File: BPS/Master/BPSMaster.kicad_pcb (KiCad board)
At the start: 2 copper layers, 100 x 75 mm, 151 parts, among them J1 SWD, J10 CurrentSlaveConnector, J11 USB_B_Micro, J12 Conn_01x06, J13 CAN Analyzer, J14 Conn_01x06, J15 Conn_01x06, J16 Conn_01x06, J2 CarPowerConnector, J3 FrontFans, J4 BackFans, J5 SPI Analyzer, J6 VoltageSlaveConnector, J7 ContactorConnector, J8 CAN_Out, J9 ErrorLightConnector, Q1 VND5N07-E, Q2 NTR4003NT1G, Q3 NTR4003NT1G, Q4 NTR4003NT1G, Q6 DMP3013SFV, SW1 B3SL-1002P, SW3 SW_Push, U1 STM32F413RHTx, U10 BAS70-04, U11 SI8261ABC-IS, U12 CDSOT23-T24CAN, U13 ADM3055E, U14 SI8261ABC-IS, U15 CP2102N-A01-GQFN24, U2 RI3-1205S, U3 NCP1117-3.3_SOT223, U4 M24128, U5 LTC6256, U8 LTC6820, U9 HX1188FNL, Y1 8M

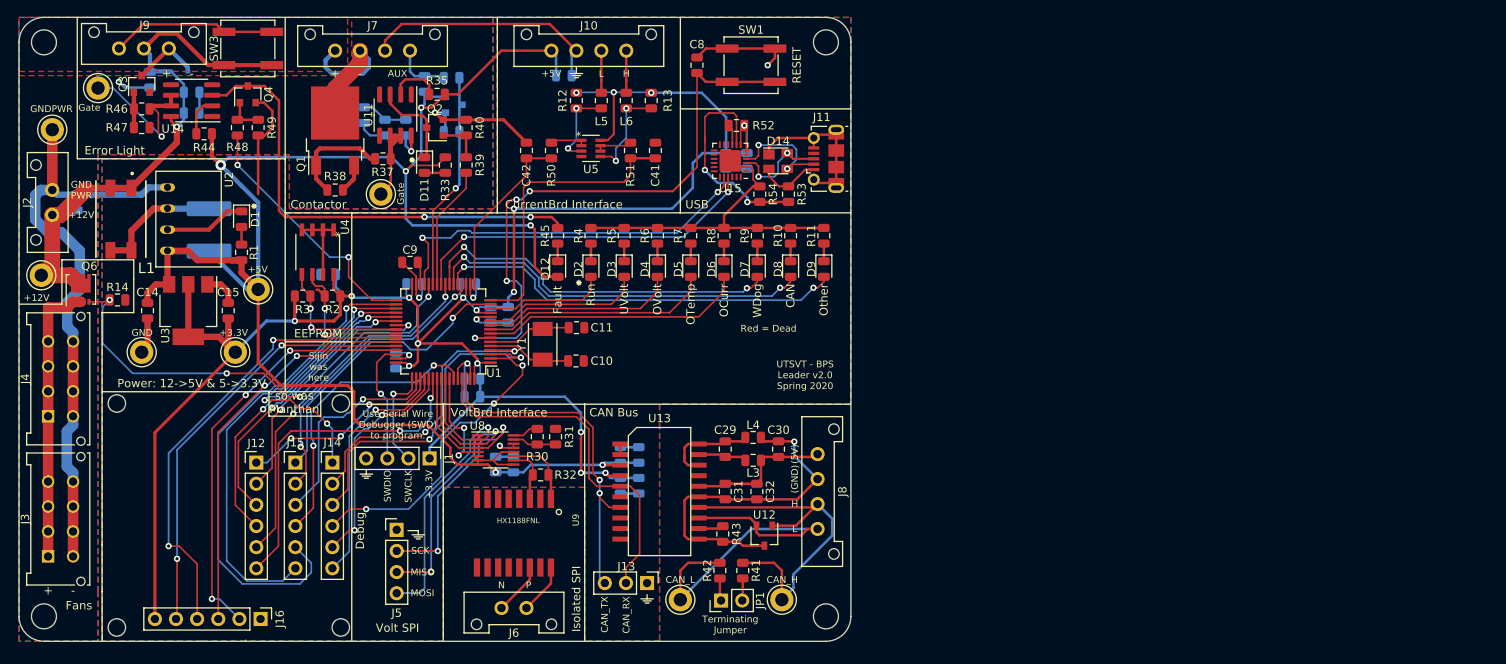
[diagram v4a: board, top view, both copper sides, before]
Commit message: Reverts edited files that are not related to the FanBoard back to master branch's versions
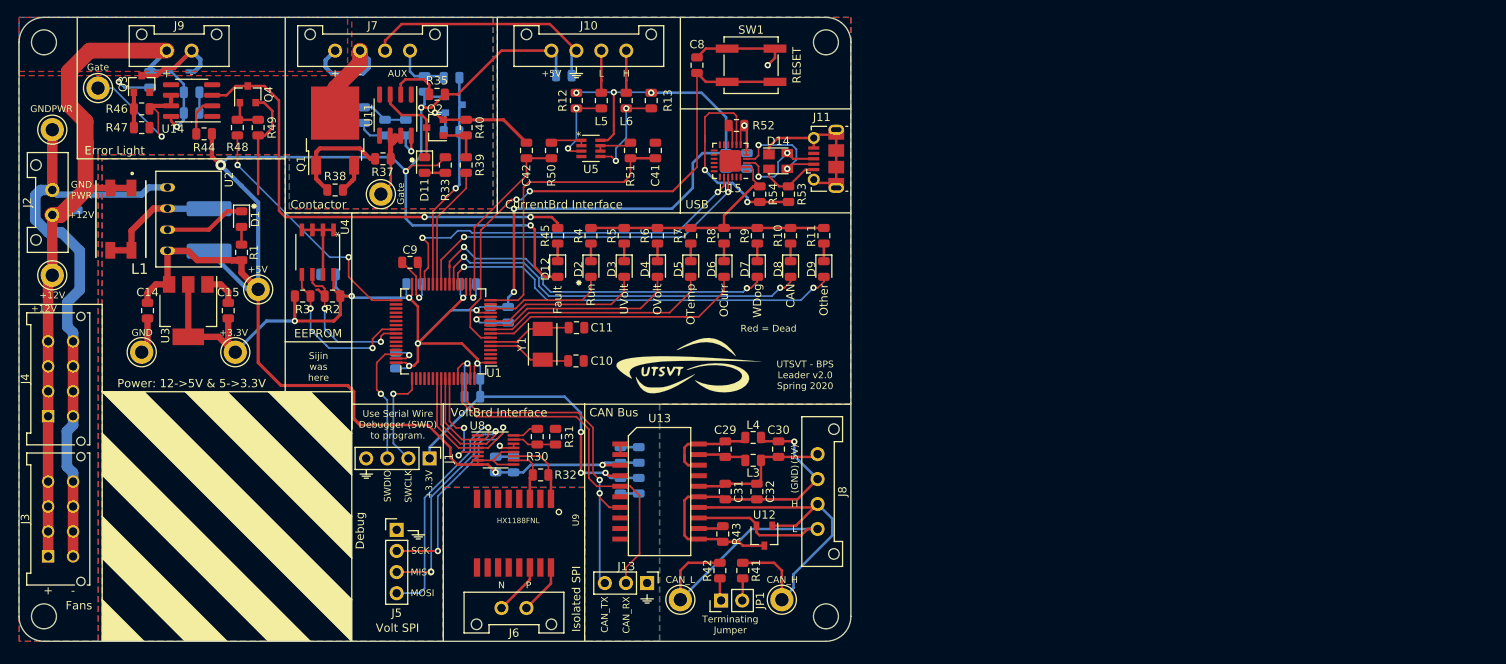
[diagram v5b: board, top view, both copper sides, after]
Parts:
- removed H1, H2, H3, H4: MountingHole, MountingHole:MountingHole_2.1mm
- removed J12, J14, J15, J16: Conn_01x06, Connector_PinHeader_2.54mm:PinHeader_1x06_P2.54mm_Vertical
- removed Q6: DMP3013SFV, Package_SON:Diodes_PowerDI3333-8
- removed R14: 10k, Resistor_SMD:R_0805_2012Metric
- removed SW3: SW_Push, Button_Switch_SMD:SW_SPST_B3SL-1002P
- added G***: LOGO, UTSVT_Special:Hallock_Image_Small, B.Cu at (184.5, 109.0)
- added G***: LOGO, UTSVT_Special:UTSVT_Logo_Symbol, F.Cu at (180.2, 117.0)
- J9: footprint UTSVT_Connectors:Molex_MicroFit3.0_1x3xP3.00mm_PolarizingPeg_Vertical -> UTSVT_Connectors:Molex_MicroFit3.0_1x2xP3.00mm_PolarizingPeg_Vertical
- moved J9 5.74 mm to (117.8, 79.0)
- moved TP1 1.32 mm to (104.0, 106.0)
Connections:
- J3 pad 1: Net-(J3-Pad1) -> +12V
- J3 pad 2: Net-(J3-Pad1) -> +12V
- J3 pad 3: Net-(J3-Pad1) -> +12V
- J3 pad 4: Net-(J3-Pad1) -> +12V
- J4 pad 1: Net-(J3-Pad1) -> +12V
- J4 pad 2: Net-(J3-Pad1) -> +12V
- J4 pad 3: Net-(J3-Pad1) -> +12V
- J4 pad 4: Net-(J3-Pad1) -> +12V
- J9 pad 1: Net-(J9-Pad1) -> +12V
- J9 pad 2: +12V -> Net-(D13-Pad2)
- U1 pad 15: /IP17 -> Net-(U1-Pad15)
- U1 pad 2: /IP8 -> Net-(U1-Pad2)
- U1 pad 20: /IP16 -> Net-(U1-Pad20)
- U1 pad 24: /IP1 -> Net-(U1-Pad24)
- U1 pad 28: /LPTIM1(PWM) -> Net-(U1-Pad28)
- U1 pad 3: /IP9 -> Net-(U1-Pad3)
- U1 pad 34: /IP13 -> Net-(U1-Pad34)
- U1 pad 35: /IP12 -> Net-(U1-Pad35)
- U1 pad 36: /IP11 -> Net-(U1-Pad36)
- U1 pad 37: /IP2 -> Net-(U1-Pad37)
- U1 pad 38: /IP3 -> Net-(U1-Pad38)
- U1 pad 39: /IP4 -> Net-(U1-Pad39)
- U1 pad 4: /IP10 -> Net-(U1-Pad4)
- U1 pad 42: /USART1_TX -> Net-(U1-Pad42)
- U1 pad 43: /USART1_RX -> Net-(U1-Pad43)
- U1 pad 44: /USART1_CTS -> Net-(U1-Pad44)
- U1 pad 45: /USART1_RTS -> Net-(U1-Pad45)
- U1 pad 50: /IP15 -> Net-(U1-Pad50)
- U1 pad 51: /IP5 -> Net-(U1-Pad51)
- U1 pad 52: /IP6 -> Net-(U1-Pad52)
- U1 pad 53: /IP7 -> Net-(U1-Pad53)
- U1 pad 54: /IP0 -> Net-(U1-Pad54)
- U1 pad 59: /IP14 -> Net-(U1-Pad59)
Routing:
- net /IP13: track 60.6 -> 0.00 mm, vias 1 -> 0
- net /LPTIM1(PWM): track 57.7 -> 0.00 mm, vias 4 -> 0
- net /USART1_TX: track 55.8 -> 0.00 mm, vias 2 -> 0
- net /IP12: track 52.6 -> 0.00 mm, vias 1 -> 0
- net /USART1_RX: track 52.1 -> 0.00 mm, vias 2 -> 0
- net /USART1_CTS: track 51.0 -> 0.00 mm, vias 3 -> 0
- net /USART1_RTS: track 47.9 -> 0.00 mm, vias 2 -> 0
- net /IP1: track 44.0 -> 0.00 mm, vias 2 -> 0
- net Net-(J3-Pad1): track 42.0 -> 0.00 mm
- net /IP9: track 40.6 -> 0.00 mm, vias 2 -> 0
- net /IP0: track 40.5 -> 0.00 mm, vias 2 -> 0
- net /IP8: track 38.2 -> 0.00 mm, vias 3 -> 0
- net /IP2: track 37.0 -> 0.00 mm, vias 2 -> 0
- net +12V: track 93.8 -> 130.9 mm
- net /IP10: track 36.2 -> 0.00 mm, vias 2 -> 0
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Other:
- board text removed: "so was Manthan"

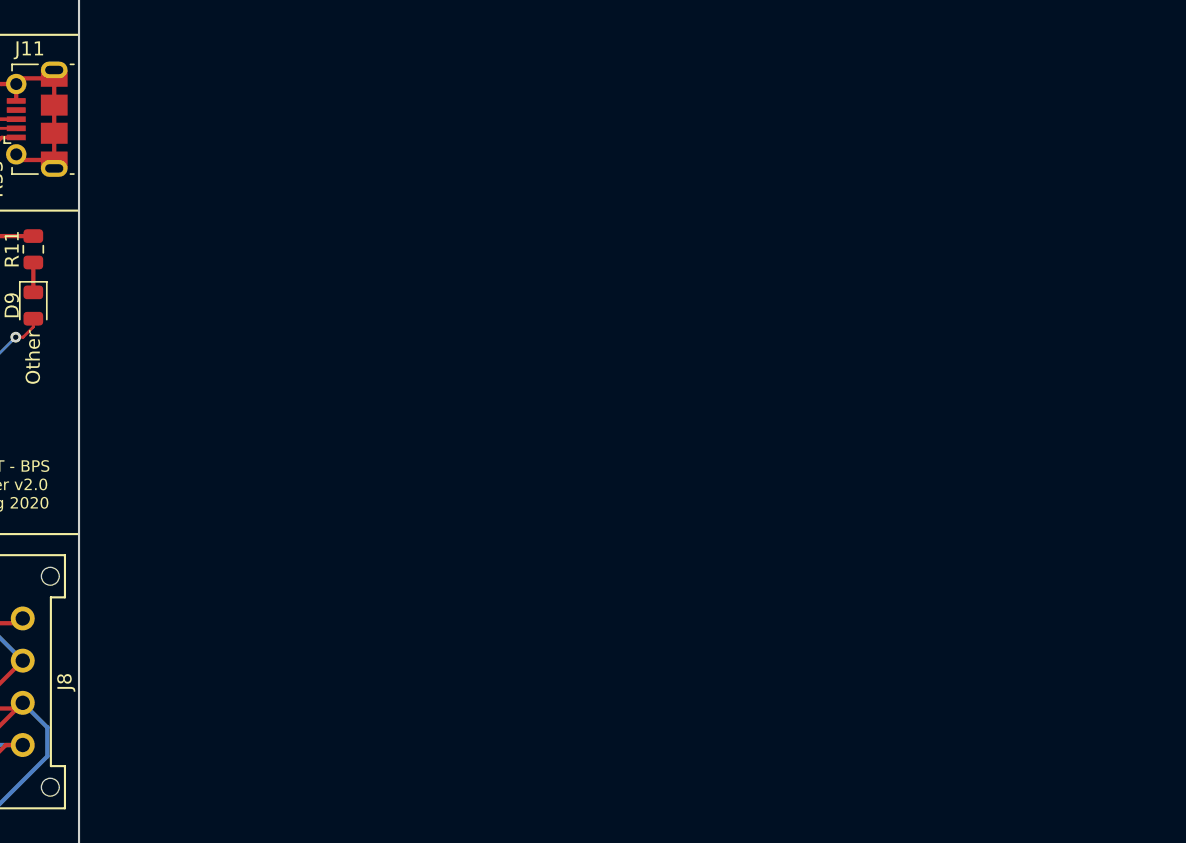
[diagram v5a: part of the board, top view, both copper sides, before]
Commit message: Made file paths of symbol libraries relative. Added footprint for high voltage detection that is SMD and has same specs as one recommended in Bluetooth Module datasheet.
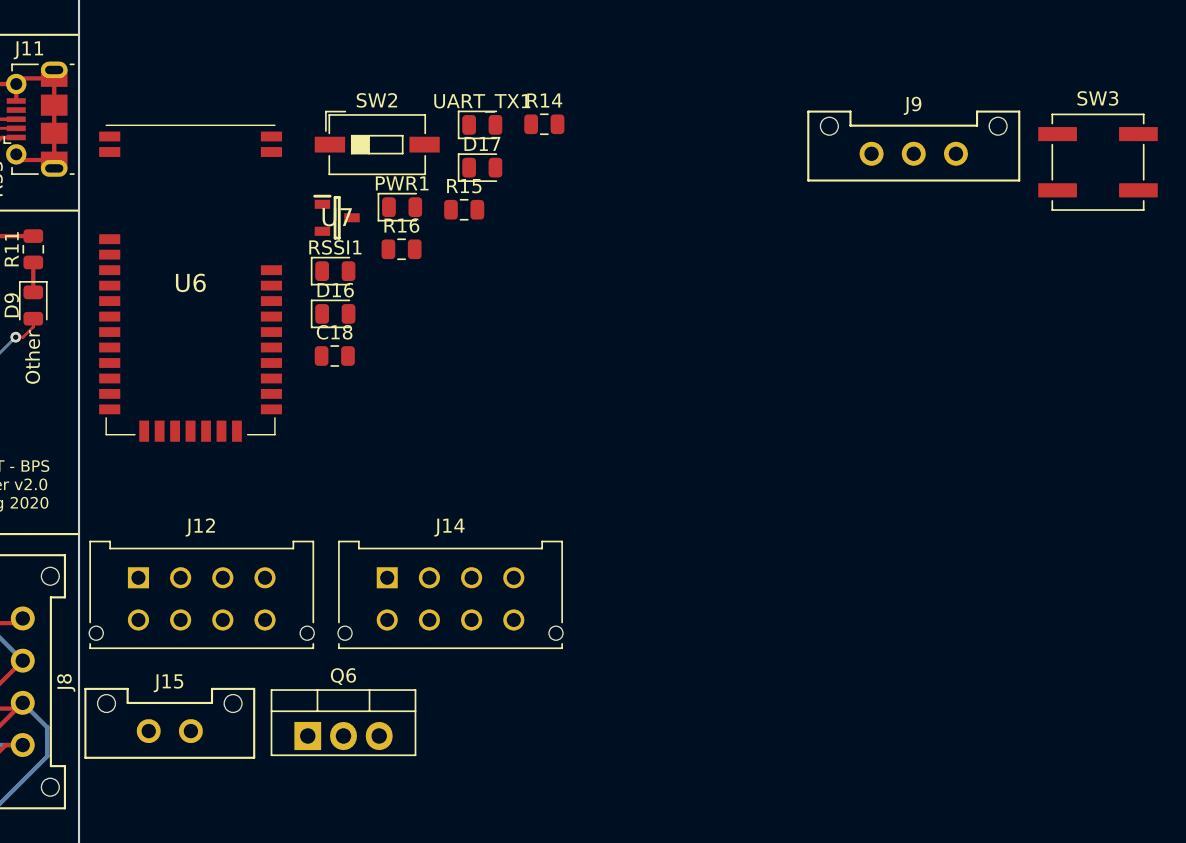
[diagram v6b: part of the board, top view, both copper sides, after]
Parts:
- added C18: 1uF, Capacitor_SMD:C_0805_2012Metric, F.Cu at (218.2, 108.8)
- added D16: LED, LED_SMD:LED_0805_2012Metric, F.Cu at (218.2, 105.8)
- added D17: LED, LED_SMD:LED_0805_2012Metric, F.Cu at (228.7, 95.4)
- added J12: Conn_01x08, UTSVT_Connectors:Molex_MicroFit3.0_2x4xP3.00mm_PolarizingPeg_Vertical, F.Cu at (204.2, 124.6)
- added J14: Conn_01x08, UTSVT_Connectors:Molex_MicroFit3.0_2x4xP3.00mm_PolarizingPeg_Vertical, F.Cu at (221.9, 124.6)
- added J15: Conn_01x02, UTSVT_Connectors:Molex_MicroFit3.0_1x2xP3.00mm_PolarizingPeg_Vertical, F.Cu at (205.0, 135.5)
- added J9: ErrorLightConnector, UTSVT_Connectors:Molex_MicroFit3.0_1x3xP3.00mm_PolarizingPeg_Vertical, F.Cu at (256.4, 94.5)
- added PWR1: LED, LED_SMD:LED_0805_2012Metric, F.Cu at (223.0, 98.3)
- added Q6: BUT11, Package_TO_SOT_THT:TO-220-3_Vertical, F.Cu at (216.3, 135.9)
- added R14: 330, Resistor_SMD:R_0805_2012Metric, F.Cu at (233.1, 92.4)
- added R15: 4.7k, Resistor_SMD:R_0805_2012Metric, F.Cu at (227.4, 98.4)
- added R16: 10k, Resistor_SMD:R_0805_2012Metric, F.Cu at (222.9, 101.2)
- added RSSI1: LED, LED_SMD:LED_0805_2012Metric, F.Cu at (218.2, 102.8)
- added SW2: SW_DIP_x01, Button_Switch_SMD:SW_DIP_SPSTx01_Slide_6.7x4.1mm_W6.73mm_P2.54mm_LowProfile_JPin, F.Cu at (221.2, 93.8)
- added SW3: SW_Push, Button_Switch_SMD:SW_SPST_B3SL-1002P, F.Cu at (272.5, 95.1)
- added U6: RN4870-V_RM118, UTSVT_BPS:RN4870IRM130, F.Cu at (207.9, 103.4)
- added U7: MCP100-315D, UTSVT_BPS:SOT96P240X110-3N, F.Cu at (218.4, 99.0)
- added UART_TX1: LED, LED_SMD:LED_0805_2012Metric, F.Cu at (228.7, 92.4)
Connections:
- J3 pad 1: +12V -> Net-(J3-Pad1)
- J3 pad 2: +12V -> Net-(J3-Pad1)
- J3 pad 3: +12V -> Net-(J3-Pad1)
- J3 pad 4: +12V -> Net-(J3-Pad1)
- J4 pad 1: +12V -> Net-(J3-Pad1)
- J4 pad 2: +12V -> Net-(J3-Pad1)
- J4 pad 3: +12V -> Net-(J3-Pad1)
- J4 pad 4: +12V -> Net-(J3-Pad1)
- U1 pad 15: Net-(U1-Pad15) -> /IP17
- U1 pad 2: Net-(U1-Pad2) -> /IP8
- U1 pad 20: Net-(U1-Pad20) -> /IP16
- U1 pad 24: Net-(U1-Pad24) -> /IP1
- U1 pad 28: Net-(U1-Pad28) -> /LPTIM1(PWM)
- U1 pad 3: Net-(U1-Pad3) -> /IP9
- U1 pad 34: Net-(U1-Pad34) -> /IP13
- U1 pad 35: Net-(U1-Pad35) -> /IP12
- U1 pad 36: Net-(U1-Pad36) -> /IP11
- U1 pad 37: Net-(U1-Pad37) -> /IP2
- U1 pad 38: Net-(U1-Pad38) -> /IP3
- U1 pad 39: Net-(U1-Pad39) -> /IP4
- U1 pad 4: Net-(U1-Pad4) -> /IP10
- U1 pad 42: Net-(U1-Pad42) -> /USART1_TX
- U1 pad 43: Net-(U1-Pad43) -> /USART1_RX
- U1 pad 44: Net-(U1-Pad44) -> /USART1_CTS
- U1 pad 45: Net-(U1-Pad45) -> /USART1_RTS
- U1 pad 50: Net-(U1-Pad50) -> /IP15
- U1 pad 51: Net-(U1-Pad51) -> /IP5
- U1 pad 52: Net-(U1-Pad52) -> /IP6
- U1 pad 53: Net-(U1-Pad53) -> /IP7
- U1 pad 54: Net-(U1-Pad54) -> /IP0
- U1 pad 59: Net-(U1-Pad59) -> /IP14
